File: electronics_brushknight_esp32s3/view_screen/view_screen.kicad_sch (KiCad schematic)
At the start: 12 parts, among them J1 Conn_01x04, J2 GC9A01, J3 Conn_01x04, J4 Conn_01x04, J5 Conn_01x04, Q1 2N7002

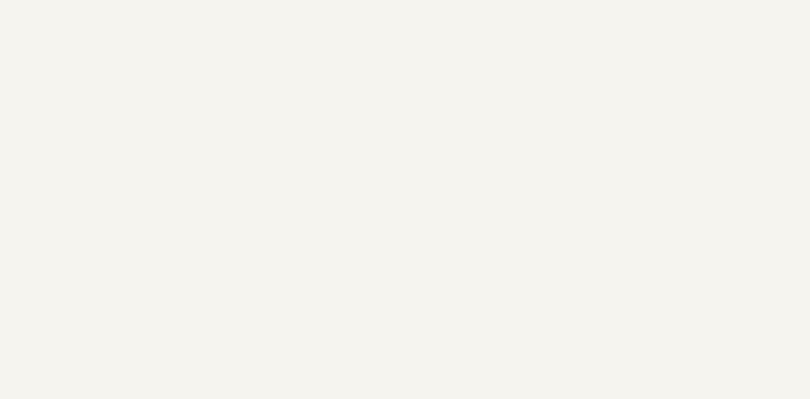
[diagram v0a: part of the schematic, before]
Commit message: updated screen PCB
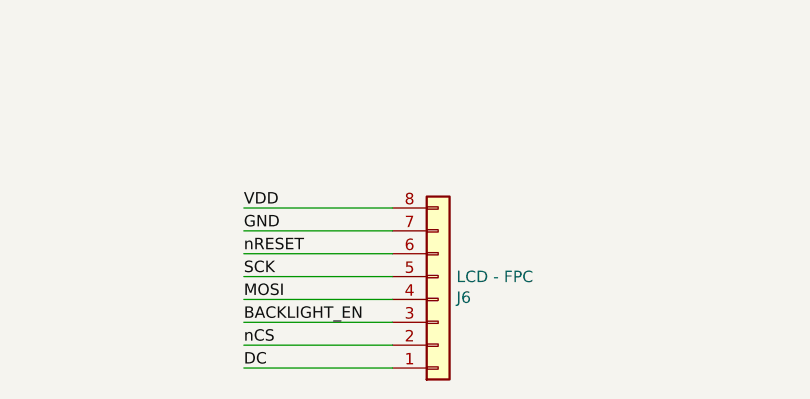
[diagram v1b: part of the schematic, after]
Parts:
- added J6: LCD - FPC, screen_connector:Amphenol FCI FPC 8 pin 0.5 pitch, symbol Connector_Generic:Conn_01x08
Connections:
- net BACKLIGHT_EN: now also J6.3 (Pin_3)
- net DC: now also J6.1 (Pin_1)
- net GND: now also J6.7 (Pin_7)
- net MOSI: now also J6.4 (Pin_4)
- net SCK: now also J6.5 (Pin_5)
- net VDD: now also J6.8 (Pin_8)
- net nCS: now also J6.2 (Pin_2)
- net nRESET: now also J6.6 (Pin_6)

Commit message: updated ibom
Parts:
- J6: Mouser (none) -> 649-59453081110EDHLF
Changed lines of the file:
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@@
+      (effects (font (size 1.27 1.27)) hide)
+    )
+    (property "Mouser" "649-59453081110EDHLF" (at 92.075 135.255 0)
       (effects (font (size 1.27 1.27)) hide)
     )
